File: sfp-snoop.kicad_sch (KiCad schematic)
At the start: 28 parts, among them J1 SFP+, J2 Conn_01x20, J3 Conn_01x20, U1 AIC1221-33GY3TR, U2 AP2191WG-7

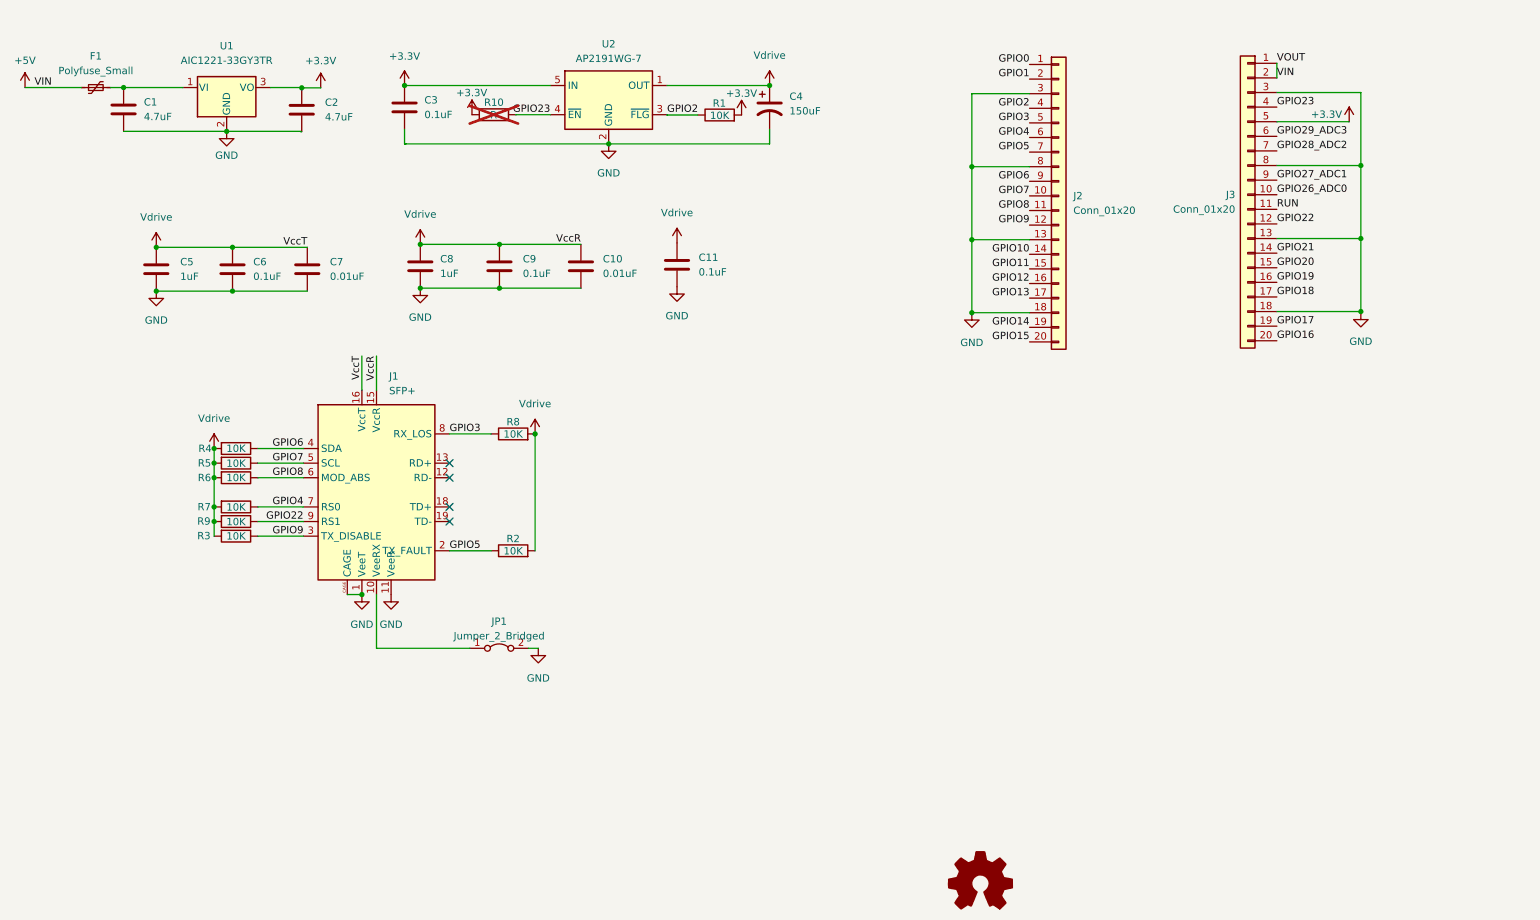
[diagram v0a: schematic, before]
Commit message: Update Nokia G-010S-A pinout
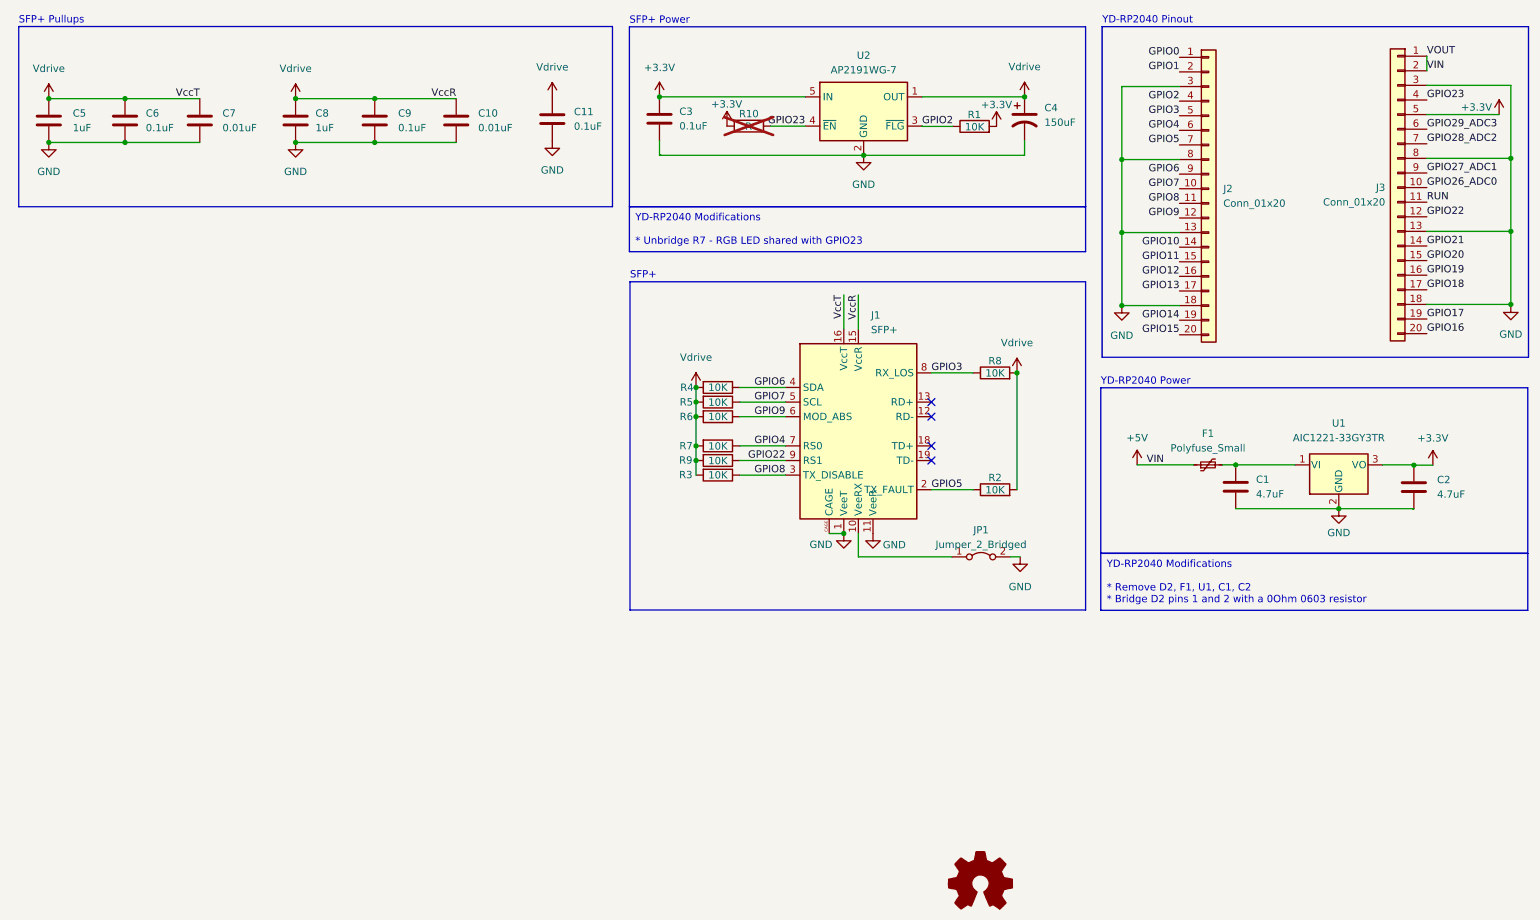
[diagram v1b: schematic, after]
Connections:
- net GPIO8: now also J1.3 (TX_DISABLE), R3.1; no longer J1.6 (MOD_ABS), R6.1
- net GPIO9: now also J1.6 (MOD_ABS), R6.1; no longer J1.3 (TX_DISABLE), R3.1
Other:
- note added: "SFP+"
- note added: "SFP+ Power"
- note added: "SFP+ Pullups"
- note added: "YD-RP2040 Pinout"
- note added: "YD-RP2040 Power"
- moved on the sheet: C1, C10, C11, C2, C3, C4, C5, C6, C7, C8, C9, F1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
